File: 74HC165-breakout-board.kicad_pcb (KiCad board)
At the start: 2 copper layers, 81 x 40 mm, 30 parts, among them J1 Conn_01x05, J10 Conn_01x04, J2 Conn_01x05, J3 Conn_01x04, J4 Conn_01x04, J5 Conn_01x04, J6 Conn_01x04, J7 Conn_01x04, J8 Conn_01x04, J9 Conn_01x04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

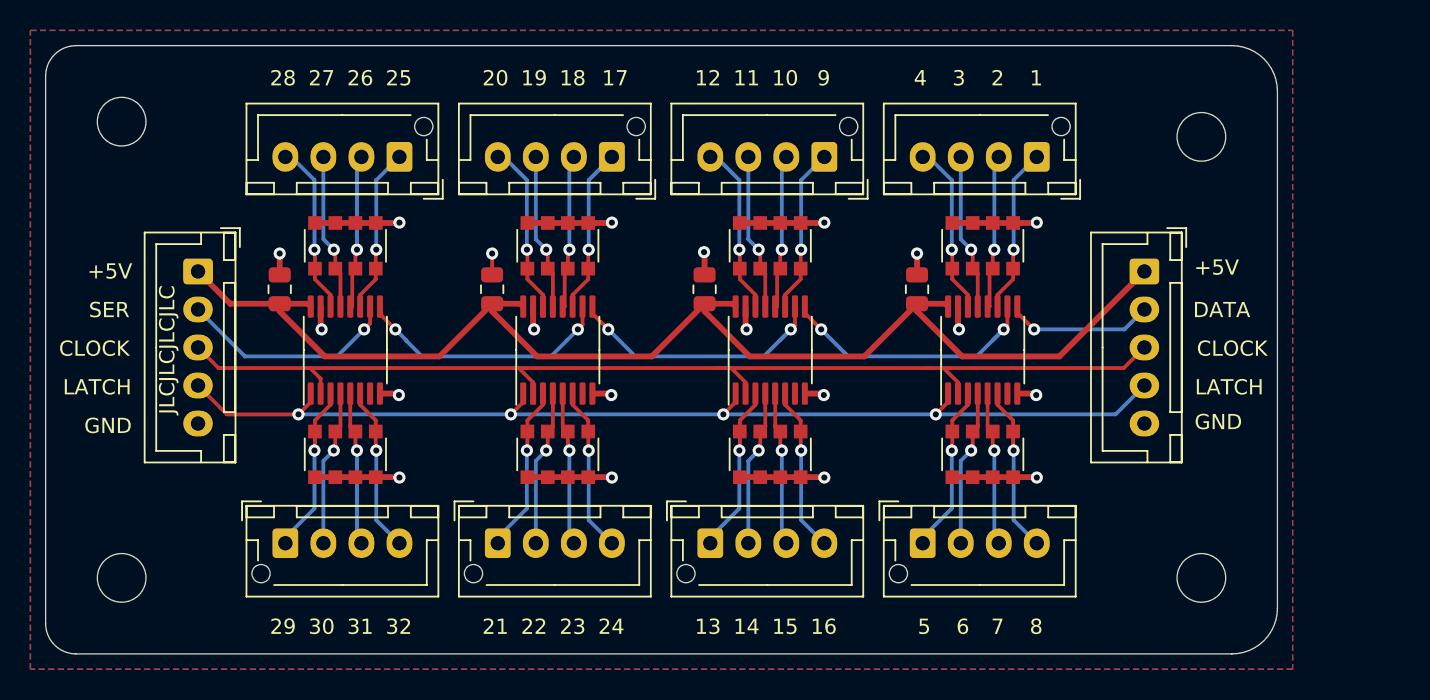
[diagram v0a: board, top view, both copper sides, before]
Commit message: Add GND to each header, remove daisy chain
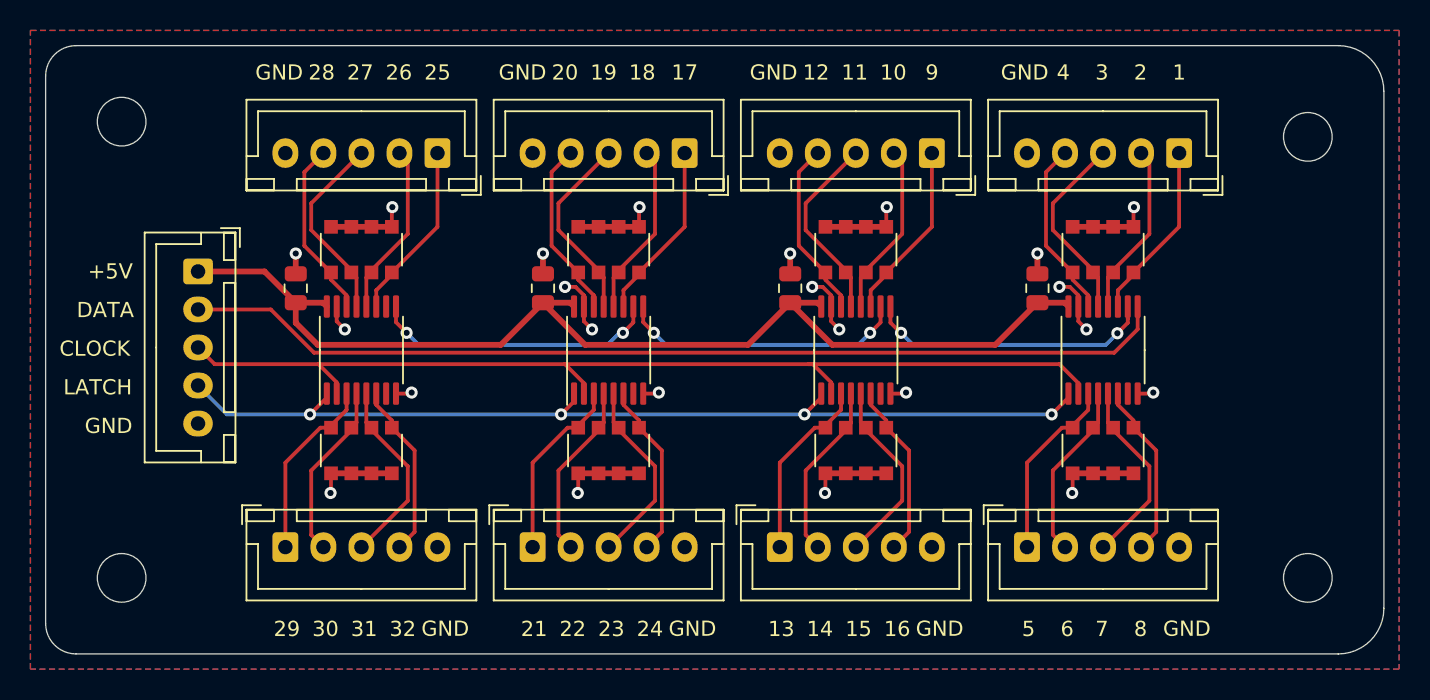
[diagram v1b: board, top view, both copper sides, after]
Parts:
- removed J10: Conn_01x04, Connector_JST:JST_XH_B4B-XH-AM_1x04_P2.50mm_Vertical
- J3, J4, J5, J6, J7, J8, J9: value Conn_01x04 -> Conn_01x05; footprint Connector_JST:JST_XH_B4B-XH-AM_1x04_P2.50mm_Vertical -> Connector_JST:JST_XH_B5B-XH-A_1x05_P2.50mm_Vertical
- moved J2 47.1 mm to (64.8, 62.1), turned to 180 degrees
- moved J8 40.1 mm to (113.5, 62.1), turned to 180 degrees
- moved J6 38.4 mm to (97.3, 62.1), turned to 180 degrees
- moved J4 36.7 mm to (81.0, 62.1), turned to 180 degrees
- moved J3 26.7 mm to (54.8, 88.0), turned to 0 degrees
- moved J5 26.2 mm to (71.0, 88.0), turned to 0 degrees
- moved J7 25.8 mm to (87.3, 88.0), turned to 0 degrees
- moved J9 25.7 mm to (103.5, 88.0), turned to 0 degrees
- moved RN7 7.92 mm to (108.5, 68.4)
- moved RN8 7.92 mm to (108.5, 81.6)
- moved C4 7.91 mm to (104.2, 71.0)
- moved U4 7.91 mm to (108.5, 75.0)
- moved H3 7.00 mm to (122.0, 61.0)
- moved H4 7.00 mm to (122.0, 90.0)
- moved RN6 5.63 mm to (92.3, 81.6)
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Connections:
- J1 pad 2: /SER -> /DATA
- J2 pad 1: +5V -> /74HC165/A
- J2 pad 2: /DATA -> /74HC165/B
- J2 pad 3: /CLOCK -> /74HC165/C
- J2 pad 4: /LATCH -> /74HC165/D
- J3 pad 1: /74HC165/A -> /74HC165/E
- J3 pad 2: /74HC165/B -> /74HC165/F
- J3 pad 3: /74HC165/C -> /74HC165/G
- J3 pad 4: /74HC165/D -> /74HC165/H
- J4 pad 1: /74HC165/E -> /sheet61DDC16C/A
- J4 pad 2: /74HC165/F -> /sheet61DDC16C/B
- J4 pad 3: /74HC165/G -> /sheet61DDC16C/C
- J4 pad 4: /74HC165/H -> /sheet61DDC16C/D
- J5 pad 1: /sheet61DDC16C/A -> /sheet61DDC16C/E
- J5 pad 2: /sheet61DDC16C/B -> /sheet61DDC16C/F
- J5 pad 3: /sheet61DDC16C/C -> /sheet61DDC16C/G
- J5 pad 4: /sheet61DDC16C/D -> /sheet61DDC16C/H
- J6 pad 1: /sheet61DDC16C/E -> /sheet61DDC3C2/A
- J6 pad 2: /sheet61DDC16C/F -> /sheet61DDC3C2/B
- J6 pad 3: /sheet61DDC16C/G -> /sheet61DDC3C2/C
- J6 pad 4: /sheet61DDC16C/H -> /sheet61DDC3C2/D
- J7 pad 1: /sheet61DDC3C2/A -> /sheet61DDC3C2/E
- J7 pad 2: /sheet61DDC3C2/B -> /sheet61DDC3C2/F
- J7 pad 3: /sheet61DDC3C2/C -> /sheet61DDC3C2/G
- J7 pad 4: /sheet61DDC3C2/D -> /sheet61DDC3C2/H
- J8 pad 1: /sheet61DDC3C2/E -> /sheet61DDC5EC/A
- J8 pad 2: /sheet61DDC3C2/F -> /sheet61DDC5EC/B
- J8 pad 3: /sheet61DDC3C2/G -> /sheet61DDC5EC/C
- J8 pad 4: /sheet61DDC3C2/H -> /sheet61DDC5EC/D
- J9 pad 1: /sheet61DDC5EC/A -> /sheet61DDC5EC/E
- J9 pad 2: /sheet61DDC5EC/B -> /sheet61DDC5EC/F
- J9 pad 3: /sheet61DDC5EC/C -> /sheet61DDC5EC/G
- J9 pad 4: /sheet61DDC5EC/D -> /sheet61DDC5EC/H
- U1 pad 10: /SER -> /74HC165/SER
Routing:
- net /DATA: track 9.75 -> 65.8 mm, vias 1 -> 0
- net GND: track 105.8 -> 65.6 mm, vias 20 -> 23
- net /SER: track 14.6 -> 0.00 mm, vias 1 -> 0
- net +5V: track 85.1 -> 72.3 mm
- net /LATCH: track 70.9 -> 64.1 mm
- net /CLOCK: track 72.8 -> 67.2 mm
- net /sheet61DDC16C/C: track 10.3 -> 12.7 mm, vias 1 -> 0
- net /sheet61DDC5EC/C: track 10.3 -> 12.7 mm, vias 1 -> 0
- net /sheet61DDC3C2/C: track 10.3 -> 12.7 mm, vias 1 -> 0
- net /74HC165/C: track 10.3 -> 12.7 mm, vias 1 -> 0
- net /74HC165/G: track 10.1 -> 12.5 mm, vias 1 -> 0
- net /sheet61DDC5EC/G: track 10.1 -> 12.5 mm, vias 1 -> 0
- net /sheet61DDC3C2/G: track 10.1 -> 12.5 mm, vias 1 -> 0
- net /sheet61DDC16C/G: track 10.1 -> 12.5 mm, vias 1 -> 0
- net /74HC165/QH: track 17.0 -> 19.2 mm
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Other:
- board size 81 x 40 mm -> 88 x 40 mm
- board text removed: "JLCJLCJLCJLC"
- board text removed: "SER"

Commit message: Switch to footprints available at JLCPCB
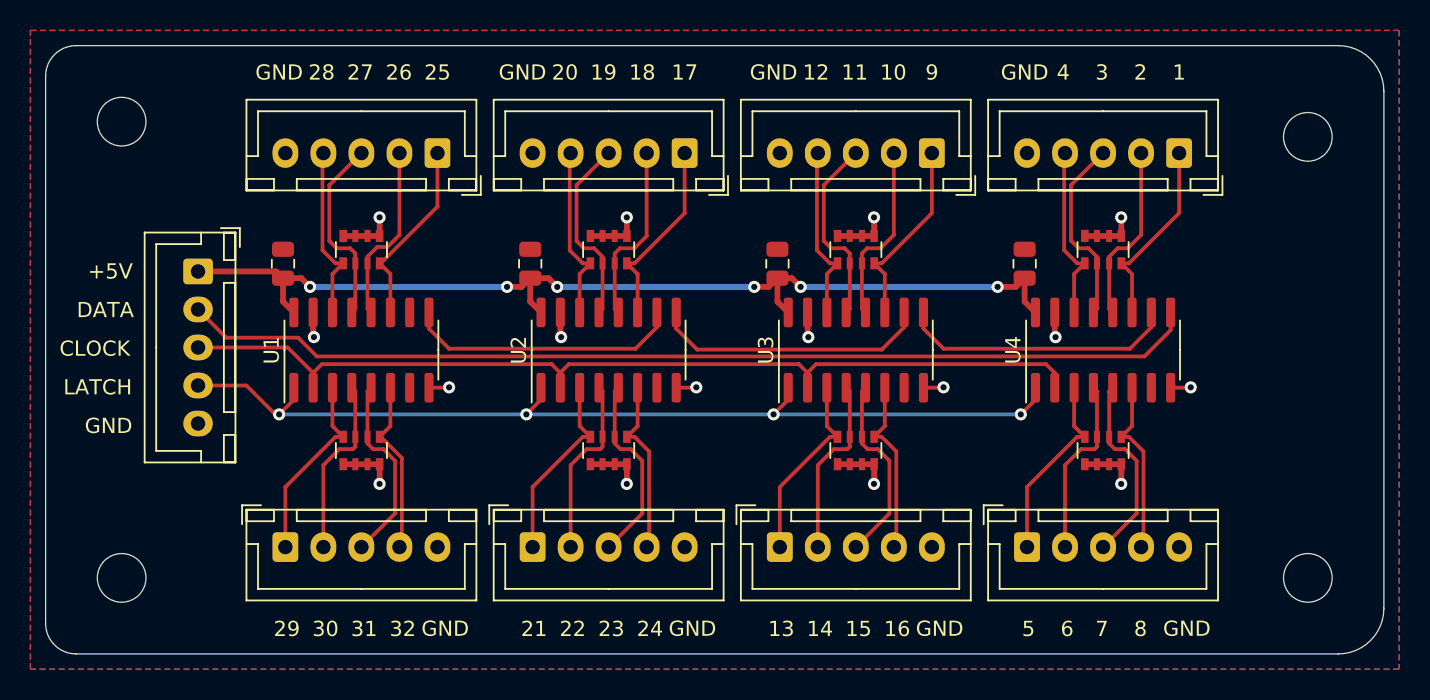
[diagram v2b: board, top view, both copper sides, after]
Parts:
- C1, C2, C3, C4: value 0.1uF -> 100nF
- RN1, RN2, RN3, RN4, RN5, RN6, RN7, RN8: footprint Resistor_SMD:R_Array_Convex_4x1206 -> Resistor_SMD:R_Array_Convex_4x0603
- U1, U2, U3, U4: footprint Package_SO:TSSOP-16_4.4x5mm_P0.65mm -> Package_SO:SOIC-16_3.9x9.9mm_P1.27mm
- moved C1 1.82 mm to (54.6, 69.3)
- moved C2 1.82 mm to (70.9, 69.3)
- moved C3 1.82 mm to (87.1, 69.3)
- moved C4 1.82 mm to (103.4, 69.3)
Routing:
- net GND: track 65.6 -> 41.2 mm, vias 23 -> 16
- net +5V: track 72.3 -> 66.2 mm, vias 0 -> 6
- net /CLOCK: track 67.2 -> 65.1 mm
- net /DATA: track 65.8 -> 67.1 mm
- net /74HC165/QH: track 19.2 -> 18.2 mm, vias 2 -> 0
- net /sheet61DDC16C/QH: track 19.1 -> 18.2 mm, vias 2 -> 0
- net /sheet61DDC3C2/A: track 11.8 -> 12.6 mm
- net /sheet61DDC16C/A: track 11.8 -> 12.6 mm
- net /sheet61DDC5EC/A: track 11.8 -> 12.6 mm
- net /sheet61DDC3C2/QH: track 19.0 -> 18.2 mm, vias 2 -> 0
- net /74HC165/A: track 11.8 -> 12.4 mm
- net /LATCH: track 64.1 -> 63.5 mm
- net /sheet61DDC16C/B: track 11.4 -> 12.0 mm
- net /sheet61DDC3C2/B: track 11.4 -> 12.0 mm

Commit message: Fix resistors, add tooling holes, add test points
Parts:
- added H5: MountingHole, 74HC165-breakout-board:JLCPCB_Tooling_Hole, F.Cu at (42.0, 65.1)
- added H6: MountingHole, 74HC165-breakout-board:JLCPCB_Tooling_Hole, F.Cu at (42.0, 85.0)
- added H7: MountingHole, 74HC165-breakout-board:JLCPCB_Tooling_Hole, F.Cu at (124.0, 85.1)
- added J10: Conn_01x04, Connector_PinHeader_2.54mm:PinHeader_1x04_P2.54mm_Vertical, F.Cu at (117.3, 71.6)
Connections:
- net /CLOCK renamed CLOCK
- net /DATA renamed DATA
- net /LATCH renamed LATCH
- RN1 pad 1: GND -> +5V
- RN1 pad 2: GND -> +5V
- RN1 pad 3: GND -> +5V
- RN1 pad 4: GND -> +5V
- RN2 pad 1: GND -> +5V
- RN2 pad 2: GND -> +5V
- RN2 pad 3: GND -> +5V
- RN2 pad 4: GND -> +5V
- RN3 pad 1: GND -> +5V
- RN3 pad 2: GND -> +5V
- RN3 pad 3: GND -> +5V
- RN3 pad 4: GND -> +5V
- RN4 pad 1: GND -> +5V
- RN4 pad 2: GND -> +5V
- RN4 pad 3: GND -> +5V
- RN4 pad 4: GND -> +5V
- RN5 pad 1: GND -> +5V
- RN5 pad 2: GND -> +5V
- RN5 pad 3: GND -> +5V
- RN5 pad 4: GND -> +5V
- RN6 pad 1: GND -> +5V
- RN6 pad 2: GND -> +5V
- RN6 pad 3: GND -> +5V
- RN6 pad 4: GND -> +5V
- RN7 pad 1: GND -> +5V
- RN7 pad 2: GND -> +5V
- RN7 pad 3: GND -> +5V
- RN7 pad 4: GND -> +5V
- RN8 pad 1: GND -> +5V
- RN8 pad 2: GND -> +5V
- RN8 pad 3: GND -> +5V
- RN8 pad 4: GND -> +5V
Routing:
- net +5V: track 66.2 -> 191.9 mm, vias 6 -> 12
- net GND: track 41.2 -> 11.9 mm, vias 16 -> 8
- net LATCH: track 63.5 -> 78.8 mm
- net CLOCK: track 65.1 -> 78.0 mm
- net DATA: track 67.1 -> 71.9 mm
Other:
- board text added: "0"
- board text added: "JLCJLCJLCJLC"
- board text added: "Test points"
- board text removed: "32"

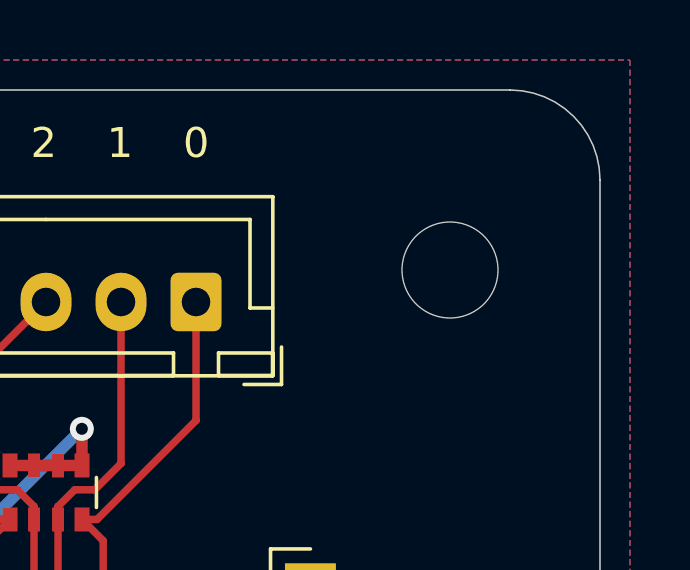
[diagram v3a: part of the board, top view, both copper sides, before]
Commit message: Add PCB measurements
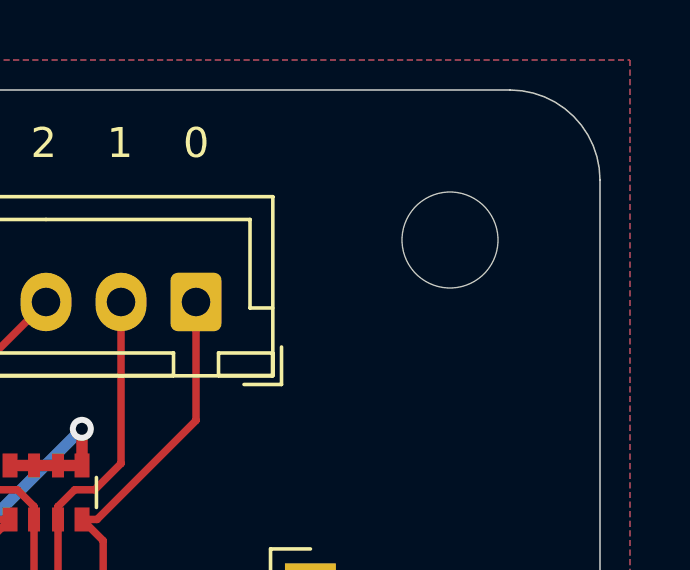
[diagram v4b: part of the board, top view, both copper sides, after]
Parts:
- moved H3 1.00 mm to (122.0, 60.0)

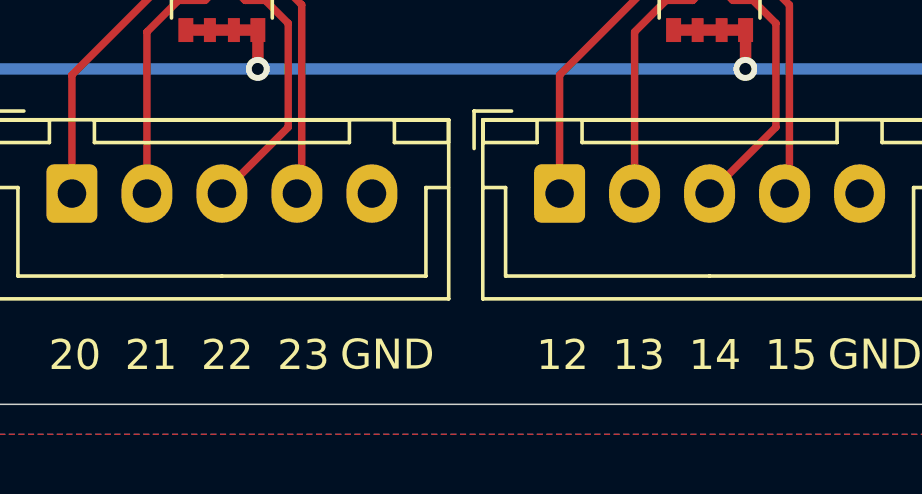
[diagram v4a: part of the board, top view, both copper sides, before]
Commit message: Add version and date stamps
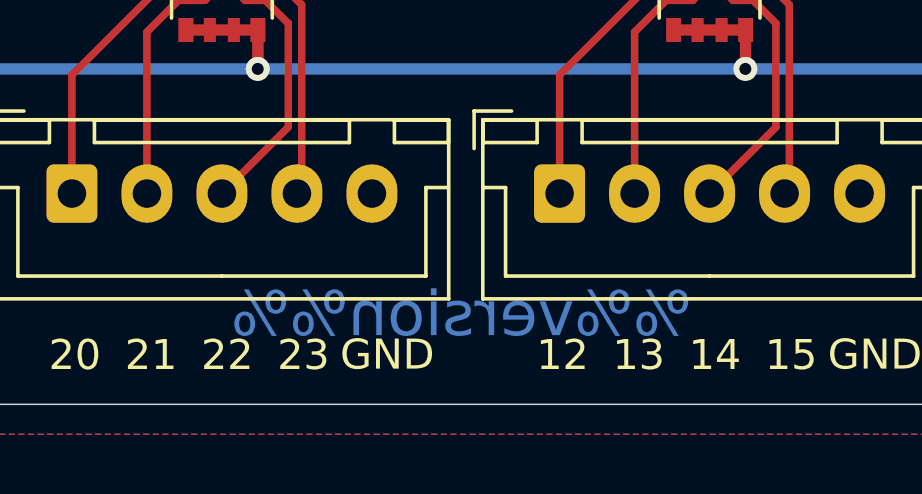
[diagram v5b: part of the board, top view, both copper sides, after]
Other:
- board text added: "%%date%%"
- board text added: "%%version%%"
- board text added: "74HC165 breakout board"
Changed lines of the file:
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@@
   (general
     (thickness 1.6)
-    (drawings 67)
+    (drawings 71)
     (tracks 372)
     (zones 0)
@@
   )
   (page A4)
+  (title_block
+    (date %%date%%)
+    (rev %%version%%)
+    (comment 2 neile@live.com)
+    (comment 3 "Neil Enns")
+    (comment 4 "74HC165 breakout board")
+  )
   (layers
-    (0 F.Cu signal)
+    (0 F.Cu signal hide)
     (31 B.Cu signal)
-    (32 B.Adhes user)
-    (33 F.Adhes user)
+    (32 B.Adhes user hide)
+    (33 F.Adhes user hide)
     (34 B.Paste user)
-    (35 F.Paste user)
+    (35 F.Paste user hide)
     (36 B.SilkS user)
-    (37 F.SilkS user)
+    (37 F.SilkS user hide)
     (38 B.Mask user)
-    (39 F.Mask user)
-    (40 Dwgs.User user)
-    (41 Cmts.User user)
-    (42 Eco1.User user)
-    (43 Eco2.User user)
+    (39 F.Mask user hide)
+    (40 Dwgs.User user hide)
+    (41 Cmts.User user hide)
+    (42 Eco1.User user hide)
+    (43 Eco2.User user hide)
     (44 Edge.Cuts user)
-    (45 Margin user)
+    (45 Margin user hide)
     (46 B.CrtYd user)
-    (47 F.CrtYd user)
+    (47 F.CrtYd user hide)
     (48 B.Fab user)
     (49 F.Fab user hide)
@@
     )
   )
+  (gr_text %%version%% (at 84 92) (layer B.Cu)
+    (effects (font (size 1.5 1.5) (thickness 0.3)) (justify mirror))
+  )
+  (gr_text %%date%% (at 60 58) (layer B.SilkS)
+    (effects (font (size 1 1) (thickness 0.15)) (justify mirror))
+  )
+  (gr_text %%version%% (at 84 58) (layer B.SilkS)
+    (effects (font (size 1 1) (thickness 0.15)) (justify mirror))
+  )
+  (gr_text "74HC165 breakout board" (at 109 58) (layer B.SilkS)
+    (effects (font (size 1 1) (thickness 0.15)) (justify mirror))
+  )
   (dimension 40 (width 0.15) (layer Dwgs.User)

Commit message: Get rid of date and version from PCB page settings, add MF logo
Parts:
- added G***: LOGO, 74HC165-breakout-board:MobiFlight_logo_BSilk, F.Cu at (50.0, 89.0)

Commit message: Add date and version back to PCB
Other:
- board text added: "adsf asdf"
- board text removed: "%%date%%"

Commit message: Add date back to PCB silkscreen
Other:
- board text added: "%%date%%"
- board text removed: "adsf asdf"
